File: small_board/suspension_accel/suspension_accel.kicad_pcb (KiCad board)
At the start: 2 copper layers, 20 x 76 mm, 10 parts, among them IC1 TJA1050T_CM,118, IC2 AMS1117-3.3, IC3 ESP32-S3-MINI-1-N8, J1 OSTTE040104

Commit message: small_board work, added buttons
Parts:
- added J2: BM04B-GVHS-TB_LF__SN_, Library:BM04BGVHSTBLFSN, F.Cu at (36.8, 69.9)
- added R4: RR0816P-103-D, Library:RESC1608X60N, F.Cu at (63.4, 63.2)
- added REF**: MountingHole_3.2mm_M3_Pad, MountingHole:MountingHole_3.2mm_M3_Pad, F.Cu at (27.0, 38.2)
- added REF**: MountingHole_3.2mm_M3_Pad, MountingHole:MountingHole_3.2mm_M3_Pad, F.Cu at (27.0, 75.5)
- added S1: TL3301FF160QG, Library:TL3301FF160QG, F.Cu at (59.5, 50.3)
- added S2: TL3301FF160QG, Library:TL3301FF160QG, F.Cu at (58.5, 31.6)
- moved R3 21.8 mm to (29.9, 52.7), turned to 180 degrees
- moved CAN_LED1 20.4 mm to (25.4, 56.2)
- moved R2 15.9 mm to (29.9, 56.2)
- moved BLINK_LED1 15.4 mm to (25.2, 52.9), turned to 180 degrees
- moved IC2 9.75 mm to (36.7, 47.5), turned to 0 degrees
- moved PWR_LED1 8.11 mm to (25.4, 59.2), turned to 0 degrees
- moved R1 5.69 mm to (29.8, 59.1), turned to 0 degrees
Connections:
- IC3 pad 39: unconnected-(IC3-TXD0-Pad39) -> Net-(IC3-TXD0)
- IC3 pad 4: unconnected-(IC3-IO0-Pad4) -> Net-(IC3-IO0)
- IC3 pad 40: unconnected-(IC3-RXD0-Pad40) -> Net-(IC3-RXD0)
- IC3 pad 45: unconnected-(IC3-EN-Pad45) -> Net-(IC3-EN)

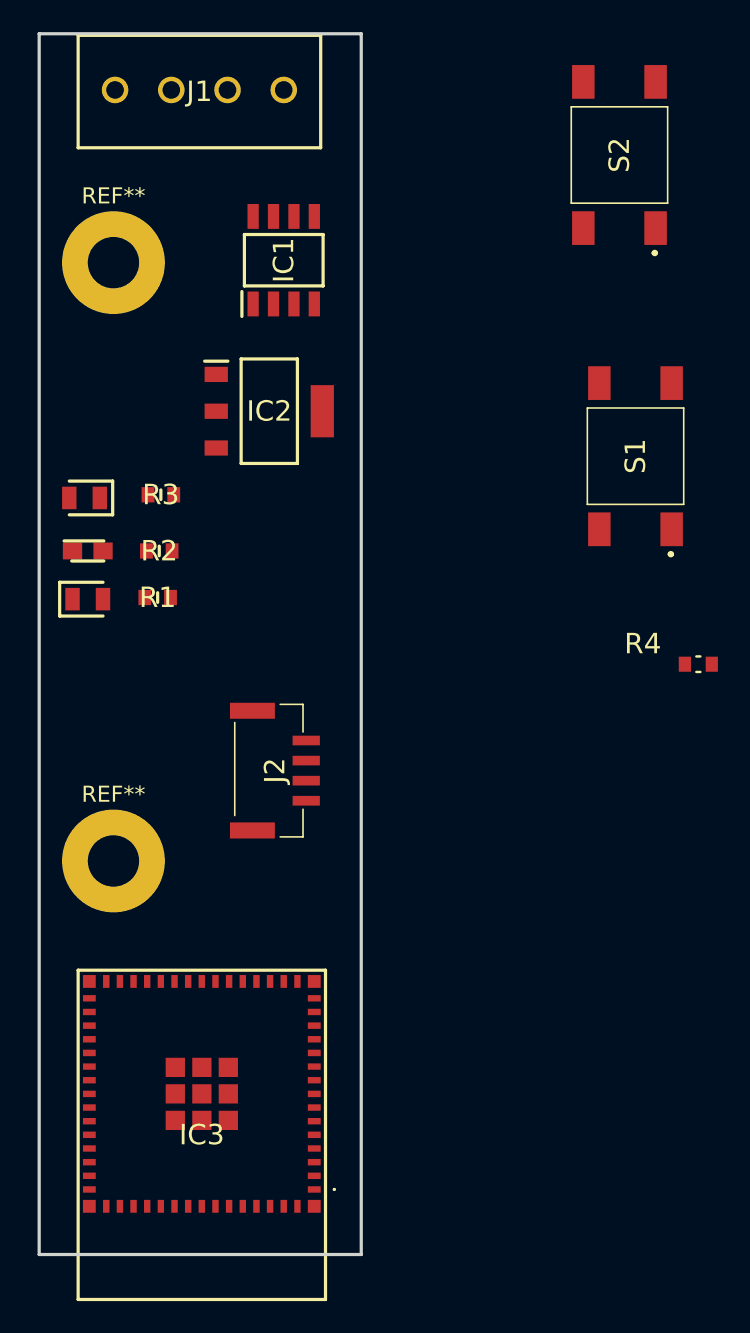
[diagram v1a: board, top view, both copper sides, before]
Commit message: added MPU, smaller buttons, started routing
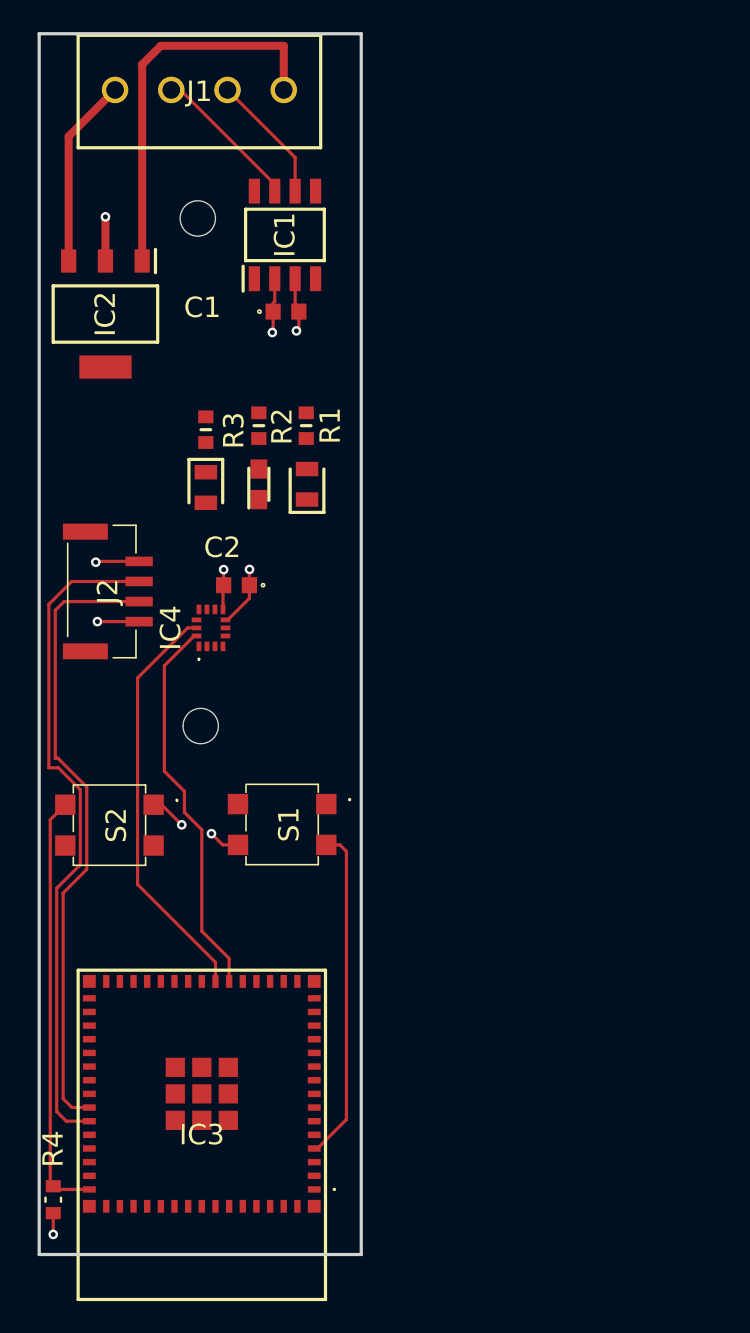
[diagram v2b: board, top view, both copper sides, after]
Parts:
- removed the REF** at (27.0, 38.2)
- removed the REF** at (27.0, 75.5)
- added C1: C0603C104K5RACTU, Library:C0603, F.Cu at (37.7, 41.3)
- added C2: C0603C104K5RACTU, Library:C0603, F.Cu at (34.7, 58.3)
- added IC4: LSM6DSV16BXTR, Library:LSM6DSV16BXTR, F.Cu at (33.1, 61.0)
- added REF**: MountingHole_2.2mm_M2, MountingHole:MountingHole_2.2mm_M2, F.Cu at (32.4, 67.1)
- added REF**: MountingHole_2.2mm_M2, MountingHole:MountingHole_2.2mm_M2, F.Cu at (32.2, 35.5)
- S1, S2: value TL3301FF160QG -> 7914G-1-032E; footprint Library:TL3301FF160QG -> Library:7914G1032E
- moved S2 52.4 mm to (26.8, 73.3), turned to -90 degrees
- moved R4 52.2 mm to (23.2, 96.6), turned to -90 degrees
- moved S1 31.8 mm to (37.5, 73.2), turned to -90 degrees
- moved PWR_LED1 15.4 mm to (39.0, 52.0), turned to 90 degrees
- moved J2 15.2 mm to (26.4, 58.7)
- moved R1 14.1 mm to (39.0, 48.4), turned to 90 degrees
- moved IC2 11.9 mm to (26.5, 41.5), turned to -90 degrees
- moved CAN_LED1 11.4 mm to (36.0, 52.0), turned to 90 degrees
- moved R2 9.96 mm to (36.0, 48.4), turned to 90 degrees
- moved BLINK_LED1 7.58 mm to (32.8, 52.2), turned to -90 degrees
- moved R3 4.92 mm to (32.8, 48.6), turned to -90 degrees
- moved IC1 1.58 mm to (37.7, 36.5)
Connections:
- IC3 pad 21: unconnected-(IC3-IO17-Pad21) -> Net-(IC3-IO17)
- IC3 pad 22: unconnected-(IC3-IO18-Pad22) -> Net-(IC3-IO18)
- J1 pad 1: GND -> +5V
- J1 pad 4: +5V -> GND
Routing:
- net Net-(IC3-RXD0): track 0.00 -> 41.8 mm
- net Net-(IC3-TXD0): track 0.00 -> 39.2 mm
- net GND: track 0.00 -> 38.7 mm, vias 0 -> 5
- net Net-(IC3-EN): track 0.00 -> 26.5 mm
- net Net-(IC3-IO18): track 0.00 -> 25.9 mm
- net Net-(IC3-IO17): track 0.00 -> 24.1 mm
- net Net-(IC3-IO0): track 0.00 -> 20.9 mm
- net +5V: track 0.00 -> 18.2 mm, vias 0 -> 2
- net Net-(IC1-CANH): track 0.00 -> 9.30 mm
- net Net-(IC1-CANL): track 0.00 -> 8.04 mm
- net +3.3V: track 0.00 -> 4.07 mm, vias 0 -> 2
- net Net-(IC4-VDD): track 0.00 -> 2.50 mm, vias 0 -> 1
